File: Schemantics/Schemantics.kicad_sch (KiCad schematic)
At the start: 13 parts, among them J1 Conn_01x04, J2 Conn_01x02, Q1 BC547, U1 ESP32-WROOM-32D

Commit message: schemantic update
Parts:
- R3: value 1000R -> 10000R
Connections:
- net at J2.2 (Pin_2), R3.1, R4.1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: no longer U1.26 (IO4)
- net at Q1.1 (C), R3.2: now also U1.26 (IO4)
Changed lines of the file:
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@@
   (junction (at 71.12 104.14) (diameter 0) (color 0 0 0 0)
   )
-  (junction (at 207.01 35.56) (diameter 0) (color 0 0 0 0)
+  (junction (at 139.7 68.58) (diameter 0) (color 0 0 0 0)
   )
   (junction (at 106.68 92.71) (diameter 0) (color 0 0 0 0)
@@
     (stroke (width 0) (type default))
   )
+  (wire (pts (xy 133.35 68.58) (xy 133.35 29.21))
+    (stroke (width 0) (type default))
+  )
   (wire (pts (xy 63.5 104.14) (xy 66.04 104.14))
     (stroke (width 0) (type default))
@@
     (stroke (width 0) (type default))
   )
-  (wire (pts (xy 63.5 35.56) (xy 116.84 35.56))
-    (stroke (width 0) (type default))
-  )
-  (wire (pts (xy 116.84 35.56) (xy 116.84 58.42))
+  (wire (pts (xy 116.84 50.8) (xy 116.84 58.42))
     (stroke (width 0) (type default))
   )
@@
     (stroke (width 0) (type default))
   )
+  (wire (pts (xy 133.35 29.21) (xy 217.17 29.21))
+    (stroke (width 0) (type default))
+  )
   (wire (pts (xy 139.7 35.56) (xy 139.7 58.42))
     (stroke (width 0) (type default))
@@
     (stroke (width 0) (type default))
   )
+  (wire (pts (xy 217.17 29.21) (xy 217.17 63.5))
+    (stroke (width 0) (type default))
+  )
   (wire (pts (xy 139.7 35.56) (xy 158.75 35.56))
     (stroke (width 0) (type default))
@@
     (stroke (width 0) (type default))
   )
+  (wire (pts (xy 139.7 66.04) (xy 139.7 68.58))
+    (stroke (width 0) (type default))
+  )
   (wire (pts (xy 41.91 76.2) (xy 41.91 104.14))
     (stroke (width 0) (type default))
   )
+  (wire (pts (xy 63.5 50.8) (xy 116.84 50.8))
+    (stroke (width 0) (type default))
+  )
+  (wire (pts (xy 139.7 68.58) (xy 133.35 68.58))
+    (stroke (width 0) (type default))
+  )
   (wire (pts (xy 139.7 80.01) (xy 139.7 95.25))
     (stroke (width 0) (type default))
   )
+  (wire (pts (xy 139.7 68.58) (xy 139.7 69.85))
+    (stroke (width 0) (type default))
+  )
   (wire (pts (xy 54.61 90.17) (xy 66.04 90.17))
     (stroke (width 0) (type default))
@@
     (stroke (width 0) (type default))
   )
-  (wire (pts (xy 215.9 63.5) (xy 215.9 35.56))
-    (stroke (width 0) (type default))
-  )
-  (wire (pts (xy 63.5 62.23) (xy 63.5 35.56))
-    (stroke (width 0) (type default))
-  )
-  (wire (pts (xy 139.7 66.04) (xy 139.7 69.85))
-    (stroke (width 0) (type default))
-  )
-  (wire (pts (xy 207.01 35.56) (xy 215.9 35.56))
+  (wire (pts (xy 63.5 62.23) (xy 63.5 50.8))
     (stroke (width 0) (type default))
   )
@@
     (stroke (width 0) (type default))
   )
-  (wire (pts (xy 195.58 63.5) (xy 215.9 63.5))
+  (wire (pts (xy 195.58 63.5) (xy 217.17 63.5))
     (stroke (width 0) (type default))
   )
@@
   )
   (text_box "todo: low voltage regulation via APX810S-29SA-7 ?"
-    (at 134.62 124.46 0) (size 26.67 17.78)
+    (at 127 127 0) (size 26.67 17.78)
     (stroke (width 0) (type default))
     (fill (type none))
@@
       (effects (font (size 1.27 1.27)) (justify left))
     )
-    (property "Value" "1000R" (at 142.24 63.5 0)
-      (effects (font (size 1.27 1.27)) (justify left))
-    )
+    (property "Value" "10000R" (at 142.24 63.5 0)
+      (effects (font (size 1.27 1.27)) (justify left))
+    )

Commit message: addedfull bridge rectifier to the  schematic
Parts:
- removed D1, D2, D3, D4: 1N4007, Diode_THT:D_DO-41_SOD81_P10.16mm_Horizontal, symbol Diode:1N4007
- added D7: B380C5000-3x00A, Diode_THT:Diode_Bridge_32.0x5.6x17.0mm_P10.0mm_P7.5mm, symbol Diode_Bridge:B380C5000-3x00A
- added U2: BD49LxxG, Package_TO_SOT_SMD:SOT-23, symbol Power_Management:BD49LxxG
- R1: value 20000R -> 1000R
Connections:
- net GND: now also D7.1 (-), U2.3 (GND)
- net at R3.1, R4.1, U1.2 (VDD): now also U2.1 (VOUT); no longer J2.2 (Pin_2)
- net at R1.1: now also D7.4 (+)
- net at J1.1 (Pin_1), J1.2 (Pin_2): now also D7.3
- net at J1.3 (Pin_3), J1.4 (Pin_4): now also D7.2
- new net: J2.2 (Pin_2), U2.2 (VDD)
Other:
- moved on the sheet: J1, J2

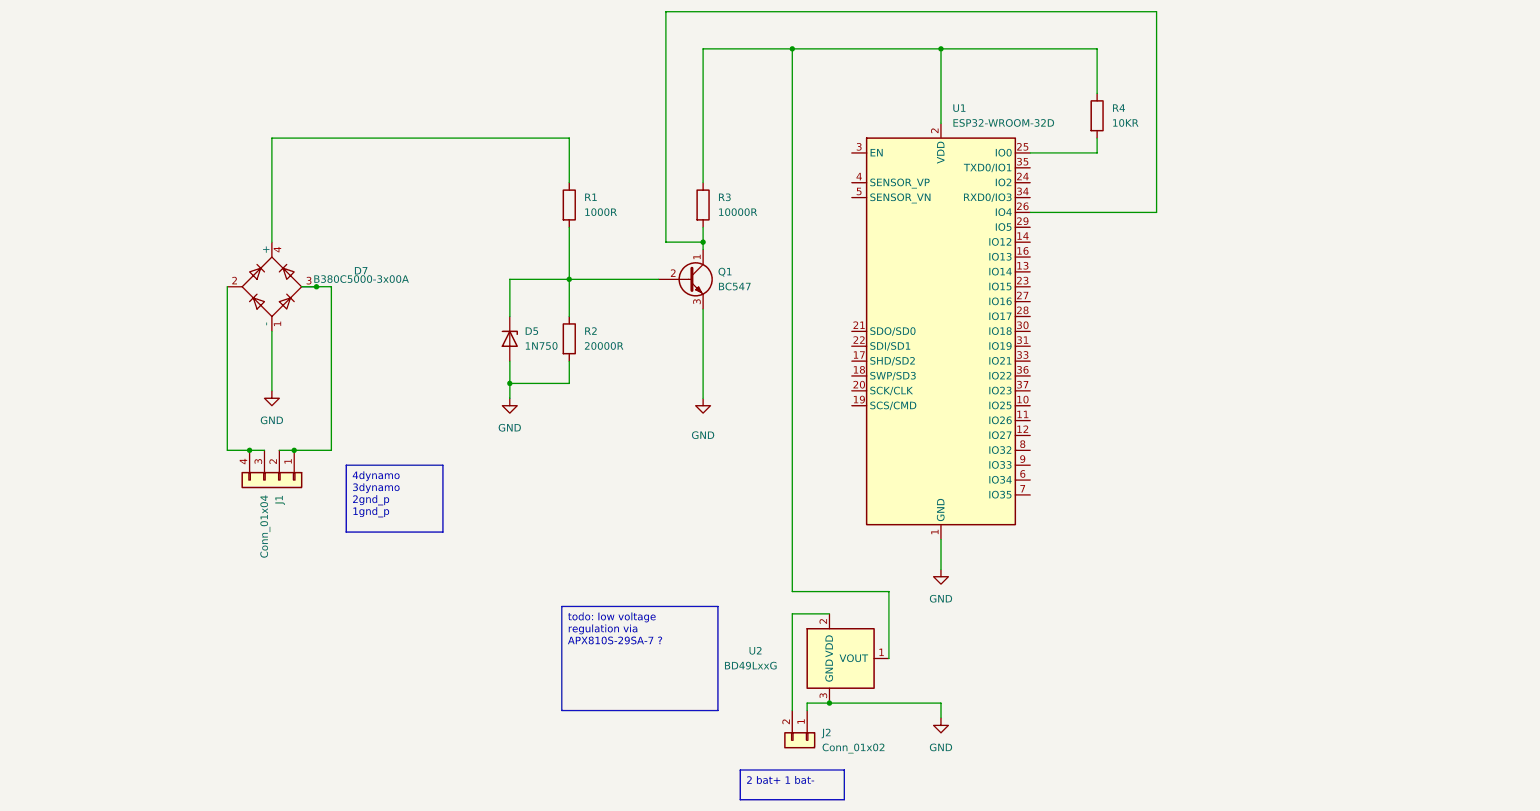
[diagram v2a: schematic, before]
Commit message: added MCP1725T-3302E/MC and debug LED
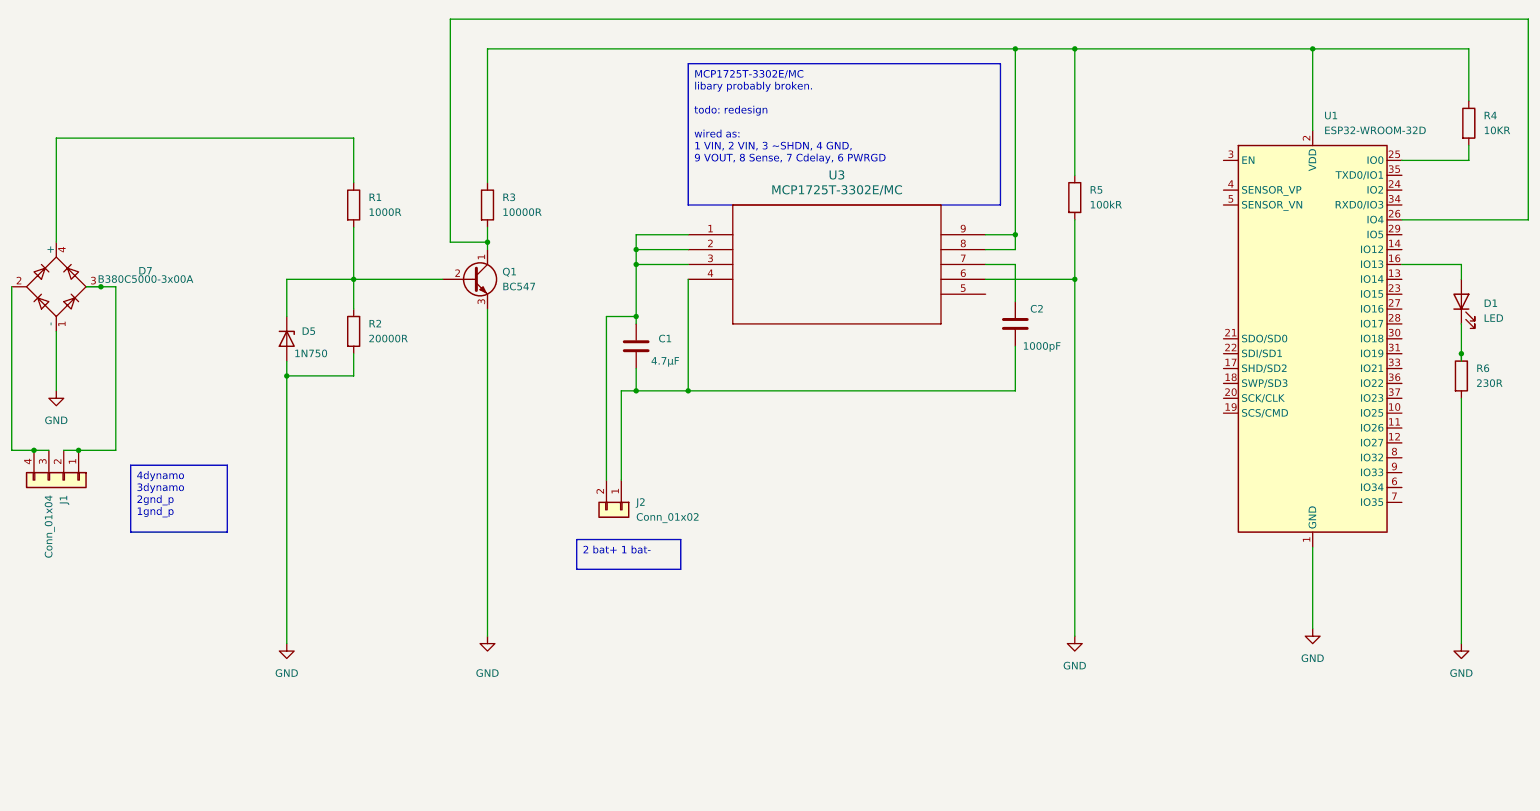
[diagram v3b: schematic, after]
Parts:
- removed U2: BD49LxxG, Package_TO_SOT_SMD:SOT-23, symbol Power_Management:BD49LxxG
- added C1: 4.7μF, Capacitor_THT:C_Rect_L16.5mm_W4.7mm_P15.00mm_MKT, symbol Device:C
- added C2: 1000pF, Capacitor_THT:C_Rect_L16.5mm_W4.7mm_P15.00mm_MKT, symbol Device:C
- added D1: LED, symbol Device:LED
- added R5: 100kR, symbol Device:R
- added R6: 230R, symbol Device:R
- added U3: MCP1725T-3302E/MC, DFN8_2x3MC_MCH, symbol test:MCP1725T-3302E_MC
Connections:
- net GND: now also R5.2, R6.2, U3.6; no longer J2.1 (Pin_1)
- net at J2.2 (Pin_2): now also C1.1, U3.1, U3.2, U3.3
- net at U1.16 (IO13): now also D1.2 (A)
- net at R3.1, R4.1, U1.2 (VDD): now also R5.1, U3.8, U3.9
- new net: D1.1 (K), R6.1
- new net: C1.2, C2.2, J2.1 (Pin_1), U3.4
- new net: C2.1, U3.7
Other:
- moved on the sheet: D5, D7, J1, J2, Q1, R1, R2, R3, R4, U1
